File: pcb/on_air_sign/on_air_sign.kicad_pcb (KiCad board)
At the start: 2 copper layers, 140 x 25 mm, 60 parts, among them J1 USB_B, J2 Conn_01x01, J3 Conn_01x01, J4 Conn_01x01, J5 Conn_01x01, J6 Conn_01x01, Q1 PN2222A, Q2 PN2222A, Q3 PN2222A

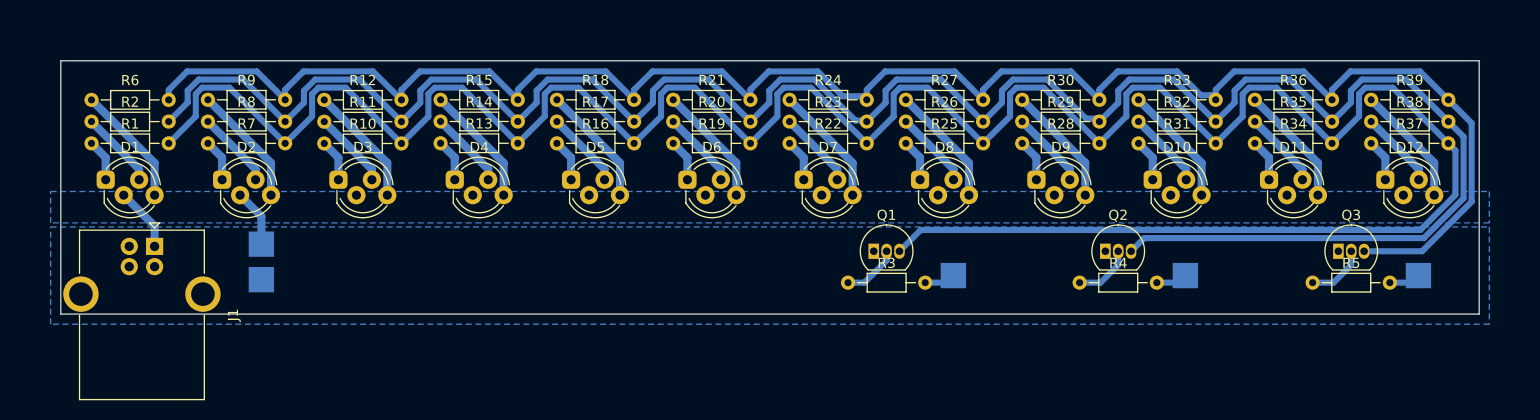
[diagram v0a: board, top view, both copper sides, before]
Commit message: update schema and board shape
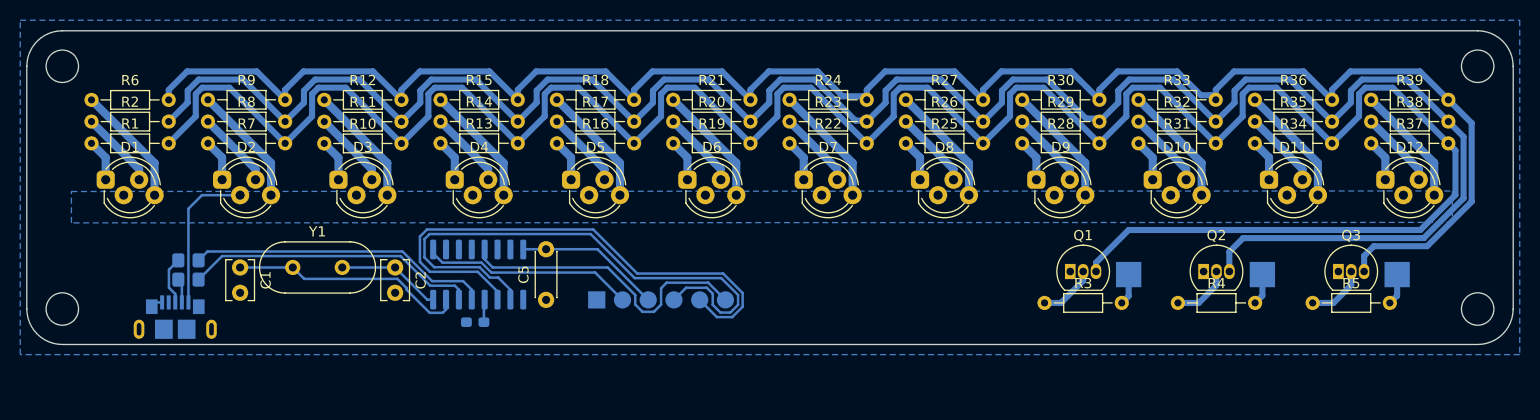
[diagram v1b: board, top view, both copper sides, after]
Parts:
- removed J3: Conn_01x01, TestPoint:TestPoint_Pad_2.5x2.5mm
- added C1: 22p, Capacitor_THT:C_Disc_D3.8mm_W2.6mm_P2.50mm, F.Cu at (67.7, 70.4)
- added C2: 22p, Capacitor_THT:C_Disc_D3.8mm_W2.6mm_P2.50mm, F.Cu at (83.0, 70.4)
- added C4: 10n, Capacitor_SMD:C_0603_1608Metric_Pad1.08x0.95mm_HandSolder, B.Cu at (90.9, 75.8)
- added C5: 100n, Capacitor_THT:C_Disc_D4.3mm_W1.9mm_P5.00mm, F.Cu at (97.9, 73.6)
- added R40: 0, Resistor_SMD:R_0805_2012Metric_Pad1.20x1.40mm_HandSolder, B.Cu at (62.6, 71.6)
- added R41: 0, Resistor_SMD:R_0805_2012Metric_Pad1.20x1.40mm_HandSolder, B.Cu at (62.6, 69.7)
- added REF**: MountingHole_3.2mm_M3, MountingHole:MountingHole_3.2mm_M3, F.Cu at (189.8, 74.5)
- added REF**: MountingHole_3.2mm_M3, MountingHole:MountingHole_3.2mm_M3, F.Cu at (50.1, 74.5)
- added REF**: MountingHole_3.2mm_M3, MountingHole:MountingHole_3.2mm_M3, F.Cu at (50.1, 50.5)
- added REF**: MountingHole_3.2mm_M3, MountingHole:MountingHole_3.2mm_M3, F.Cu at (189.8, 50.5)
- added U1: CH340G, Package_SO:SOIC-16_3.9x9.9mm_P1.27mm, B.Cu at (91.2, 71.1)
- added Y1: 12MHz, Crystal:Crystal_HC49-4H_Vertical, F.Cu at (72.9, 70.4)
- J1: value USB_B -> USB_B_Micro; footprint Connector_USB:USB_B_OST_USB-B1HSxx_Horizontal -> Connector_USB:USB_Micro-B_GCT_USB3076-30-A; moved to B.Cu
- J2: value Conn_01x01 -> SERAIL; footprint TestPoint:TestPoint_Pad_2.5x2.5mm -> Connector_PinHeader_2.54mm:PinHeader_1x06_P2.54mm_Vertical
- moved J2 33.6 mm to (102.9, 73.6), turned to 270 degrees
- moved R3 19.5 mm to (147.1, 73.9)
- moved Q1 19.5 mm to (149.6, 70.8)
- moved J4 17.3 mm to (155.4, 71.1)
- moved Q2 9.90 mm to (162.8, 70.8)
- moved R4 9.90 mm to (160.3, 73.9)
- moved J5 7.60 mm to (168.6, 71.1)
- moved J1 7.27 mm to (61.3, 75.3), turned to 180 degrees
- moved J6 2.10 mm to (181.9, 71.1)
- moved Q3 2.00 mm to (176.1, 70.8)
- moved R5 2.00 mm to (173.6, 73.9)
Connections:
- J1 pad 4: GND -> Net-(J1-Pad4)
- J1 pad 5: (no net) -> GND
- J2 pad 1: +5V -> GND
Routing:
- net /TDX: track 0.00 -> 56.0 mm
- net /RXD: track 0.00 -> 53.6 mm
- net /~DTR: track 0.00 -> 30.3 mm
- net /D+: track 0.00 -> 29.9 mm
- net /D-: track 0.00 -> 29.0 mm
- net Net-(C1-Pad1): track 0.00 -> 23.4 mm
- net /~CTS: track 0.00 -> 21.0 mm
- net /RED: track 253.2 -> 235.2 mm
- net +3V3: track 0.00 -> 14.4 mm
- net Net-(C2-Pad1): track 0.00 -> 10.4 mm
- net /GRN: track 215.0 -> 207.3 mm
- net Net-(J1-Pad3): track 0.00 -> 4.79 mm
- net +5V: track 12.0 -> 14.9 mm
- net Net-(J1-Pad2): track 0.00 -> 2.39 mm
- net Net-(C4-Pad2): track 0.00 -> 2.26 mm
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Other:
- board size 140 x 25 mm -> 146.7 x 31 mm
